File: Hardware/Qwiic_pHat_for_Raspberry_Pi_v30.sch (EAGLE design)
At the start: 26 parts, among them J1 Qwiic Right Angle, J10 RASPBERRYPI-40-PIN-GPIO_PTH_N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, J8 Qwiic Right Angle

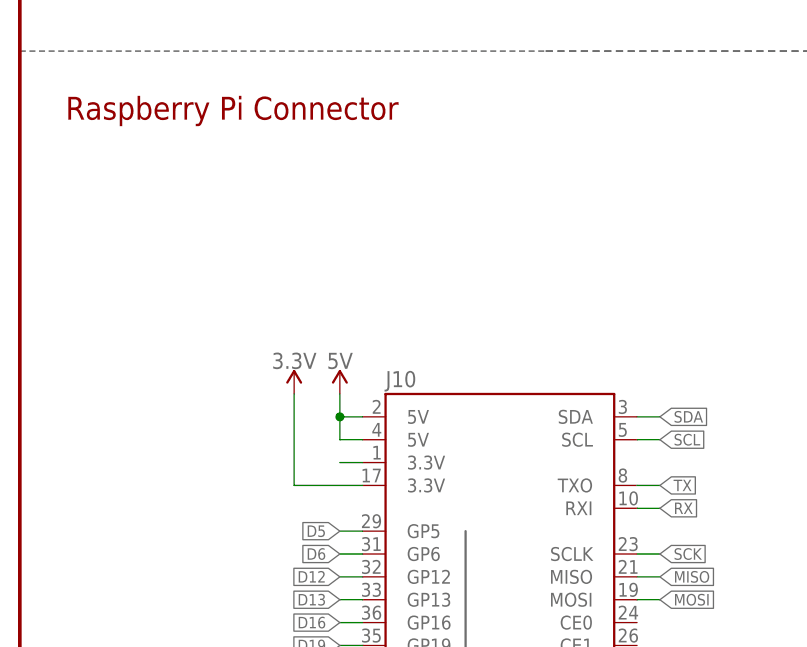
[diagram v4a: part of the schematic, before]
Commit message: Adds resettable 750mA fuse to 5V power line
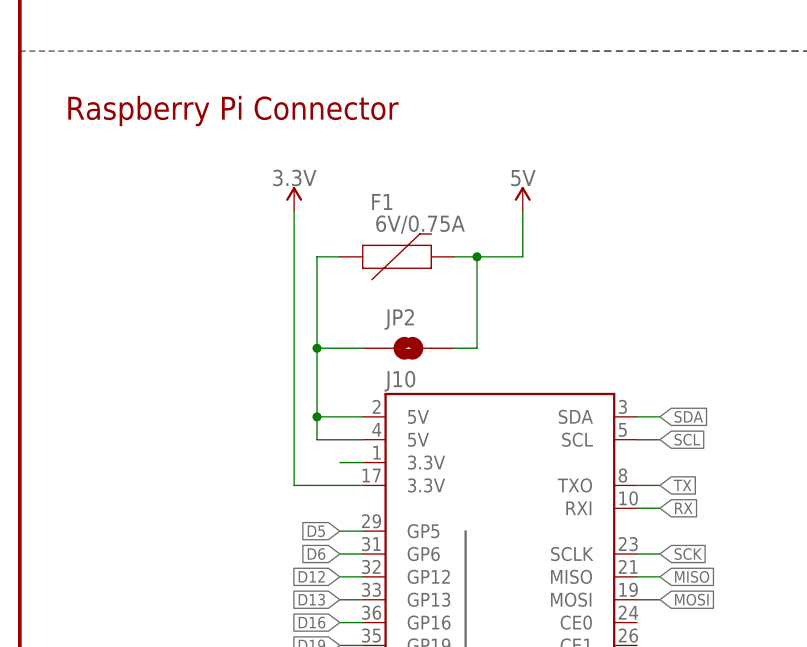
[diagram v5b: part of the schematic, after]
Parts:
- added F1: 6V/0.75A, SparkFun-Fuses:PPTC_0.75A
- added JP2: JUMPER-SMT_2_NO_NO-SILK, SparkFun-Jumpers:JUMPER-SMT_2_NO_NO-SILK
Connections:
- new net N$2: F1.1, J10.5V@2, J10.5V@4, JP2.1
- net 5V: now also F1.2, JP2.2; no longer J10.5V@2, J10.5V@4
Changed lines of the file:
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@@
 <?xml version="1.0" encoding="utf-8"?>
 <!DOCTYPE eagle SYSTEM "eagle.dtd">
-<eagle version="9.4.0">
+<eagle version="9.4.2">
 <drawing>
 <settings>
@@
 <part name="SUPPLY6" library="SparkFun-PowerSymbols" deviceset="3.3V" device=""/>
 <part name="J5" library="SparkFun-Connectors" deviceset="CONN_02" device="3.5MM-NO_SILK"/>
+<part name="F1" library="SparkFun-Fuses" deviceset="PPTC" device="_0.75A" value="6V/0.75A"/>
+<part name="JP2" library="SparkFun-Jumpers" deviceset="JUMPER-SMT_2_NO" device="_NO-SILK"/>
 </parts>
 <sheets>
@@
 <attribute name="VALUE" x="40.64" y="30.48" size="1.778" layer="96"/>
 </instance>
-<instance part="SUPPLY9" gate="G$1" x="35.56" y="93.98" smashed="yes">
-<attribute name="VALUE" x="35.56" y="96.774" size="1.778" layer="96" align="bottom-center"/>
+<instance part="SUPPLY9" gate="G$1" x="55.88" y="114.3" smashed="yes">
+<attribute name="VALUE" x="55.88" y="117.094" size="1.778" layer="96" align="bottom-center"/>
 </instance>
 <instance part="GND9" gate="1" x="35.56" y="25.4" smashed="yes">
@@
 <attribute name="VALUE" x="53.34" y="145.796" size="1.778" layer="96" font="vector" align="top-center"/>
 </instance>
-<instance part="SUPPLY2" gate="G$1" x="30.48" y="93.98" smashed="yes">
-<attribute name="VALUE" x="30.48" y="96.774" size="1.778" layer="96" align="bottom-center"/>
+<instance part="SUPPLY2" gate="G$1" x="30.48" y="114.3" smashed="yes">
+<attribute name="VALUE" x="30.48" y="117.094" size="1.778" layer="96" align="bottom-center"/>
 </instance>
 <instance part="J2" gate="G$1" x="160.02" y="157.48" smashed="yes" rot="R180">
@@
 <attribute name="VALUE" x="137.16" y="162.306" size="1.778" layer="96" font="vector" rot="MR180"/>
 <attribute name="NAME" x="137.16" y="151.892" size="1.778" layer="95" font="vector" rot="MR180"/>
+</instance>
+<instance part="F1" gate="F1" x="40.64" y="109.22" smashed="yes">
+<attribute name="NAME" x="40.259" y="116.205" size="1.778" layer="95" font="vector" rot="R180" align="bottom-center"/>
+<attribute name="VALUE" x="44.45" y="112.014" size="1.778" layer="96" font="vector" rot="R180" align="top-center"/>
+</instance>
+<instance part="JP2" gate="G$1" x="43.18" y="99.06" smashed="yes">
+<attribute name="NAME" x="40.64" y="101.6" size="1.778" layer="95" font="vector"/>
 </instance>
 </instances>
@@
 <segment>
 <pinref part="SUPPLY2" gate="G$1" pin="3.3V"/>
-<wire x1="30.48" y1="83.82" x2="30.48" y2="93.98" width="0.1524" layer="91"/>
+<wire x1="30.48" y1="83.82" x2="30.48" y2="114.3" width="0.1524" layer="91"/>
 <pinref part="J10" gate="G$1" pin="3.3V@17"/>
 <wire x1="38.1" y1="83.82" x2="30.48" y2="83.82" width="0.1524" layer="91"/>
@@
 <net name="5V" class="0">
 <segment>
-<pinref part="J10" gate="G$1" pin="5V@2"/>
-<wire x1="38.1" y1="91.44" x2="35.56" y2="91.44" width="0.1524" layer="91"/>
-<wire x1="35.56" y1="91.44" x2="35.56" y2="93.98" width="0.1524" layer="91"/>
-<pinref part="J10" gate="G$1" pin="5V@4"/>
-<wire x1="38.1" y1="88.9" x2="35.56" y2="88.9" width="0.1524" layer="91"/>
-<wire x1="35.56" y1="88.9" x2="35.56" y2="91.44" width="0.1524" layer="91"/>
-<junction x="35.56" y="91.44"/>
-<pinref part="SUPPLY9" gate="G$1" pin="5V"/>
-</segment>
-<segment>
 <pinref part="J2" gate="G$1" pin="1"/>
 <wire x1="152.4" y1="157.48" x2="149.86" y2="157.48" width="0.1524" layer="91"/>
@@
 <junction x="149.86" y="157.48"/>
 </segment>
+<segment>
+<pinref part="F1" gate="F1" pin="2"/>
+<pinref part="SUPPLY9" gate="G$1" pin="5V"/>
+<wire x1="48.26" y1="109.22" x2="50.8" y2="109.22" width="0.1524" layer="91"/>
+<pinref part="JP2" gate="G$1" pin="2"/>
+<wire x1="50.8" y1="109.22" x2="50.8" y2="99.06" width="0.1524" layer="91"/>
+<wire x1="50.8" y1="99.06" x2="48.26" y2="99.06" width="0.1524" layer="91"/>
+<junction x="50.8" y="109.22"/>
+<wire x1="50.8" y1="109.22" x2="55.88" y2="109.22" width="0.1524" layer="91"/>
+<wire x1="55.88" y1="109.22" x2="55.88" y2="114.3" width="0.1524" layer="91"/>
+</segment>
 </net>
 <net name="RX" class="0">
@@
 </segment>
 </net>
+<net name="N$2" class="0">
+<segment>
+<pinref part="J10" gate="G$1" pin="5V@2"/>
+<pinref part="J10" gate="G$1" pin="5V@4"/>
+<pinref part="F1" gate="F1" pin="1"/>
+<wire x1="35.56" y1="109.22" x2="33.02" y2="109.22" width="0.1524" layer="91"/>
+<wire x1="33.02" y1="109.22" x2="33.02" y2="99.06" width="0.1524" layer="91"/>
+<wire x1="33.02" y1="99.06" x2="33.02" y2="91.44" width="0.1524" layer="91"/>
+<wire x1="33.02" y1="91.44" x2="33.02" y2="88.9" width="0.1524" layer="91"/>
+<wire x1="33.02" y1="88.9" x2="38.1" y2="88.9" width="0.1524" layer="91"/>
+<wire x1="38.1" y1="91.44" x2="33.02" y2="91.44" width="0.1524" layer="91"/>
+<junction x="33.02" y="91.44"/>
+<pinref part="JP2" gate="G$1" pin="1"/>
+<wire x1="38.1" y1="99.06" x2="33.02" y2="99.06" width="0.1524" layer="91"/>
+<junction x="33.02" y="99.06"/>
+</segment>
+</net>

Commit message: Updates the silk
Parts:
- removed J10: RASPBERRYPI-40-PIN-GPIO_PTH_NO_SHROUD, SparkFun-Connectors:RASPBERRYPI-40-PIN-GPIO_PTH_NO_SHROUD
- added J6: (no value), SparkFun-Connectors:QWIIC_CONNECTOR
- J1: value Qwiic Right Angle -> RASPBERRYPI-40-PIN-GPIO_PTH_NO_SHROUD; device SparkFun-Connectors:I2C_STANDARDQWIIC -> SparkFun-Connectors:RASPBERRYPI-40-PIN-GPIO_PTH_NO_SHROUD
- J2: device SparkFun-Connectors:CONN_023.5MM -> SparkFun-Connectors:CONN_023.5MM-NO_SILK
- J3: device SparkFun-Connectors:QWIIC_CONNECTOR -> SparkFun-Connectors:CONN_023.5MM
- J4: value (none) -> Qwiic Right Angle; device SparkFun-Connectors:QWIIC_CONNECTOR -> SparkFun-Connectors:I2C_STANDARDQWIIC
- J5: device SparkFun-Connectors:CONN_023.5MM-NO_SILK -> SparkFun-Connectors:QWIIC_CONNECTOR
- JP1: value PULLUP -> JUMPER-SMT_2_NO_SILK; device SparkFun-Jumpers:JUMPER-SMT_3_2-NC_TRACE_NO-SILK -> SparkFun-Jumpers:JUMPER-SMT_2_NO_SILK
- JP2: value JUMPER-SMT_2_NO_NO-SILK -> PULLUP; device SparkFun-Jumpers:JUMPER-SMT_2_NO_NO-SILK -> SparkFun-Jumpers:JUMPER-SMT_3_2-NC_TRACE_NO-SILK
- LOGO1: value SFE_LOGO_NAME_FLAME.1_INCH -> REVISION; device SparkFun-Aesthetics:SFE_LOGO_NAME_FLAME.1_INCH -> SparkFun-Aesthetics:REVISION
- LOGO2: value REVISION -> OSHW-LOGOS; device SparkFun-Aesthetics:REVISION -> SparkFun-Aesthetics:OSHW-LOGOS
- LOGO3: value OSHW-LOGOS -> SFE_LOGO_NAME_FLAME.1_INCH; device SparkFun-Aesthetics:OSHW-LOGOS -> SparkFun-Aesthetics:SFE_LOGO_NAME_FLAME.1_INCH
- renumbered J8 to J7
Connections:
- net 3.3V: now also J1.3.3V@17, J5.2, J6.2, JP2.2; no longer J1.2, J10.3.3V@17, J3.2, JP1.2
- net 5V: now also J3.1, JP1.2; no longer J5.1, JP2.2
- net BUTTON/D17: now also J1.GP17; no longer J10.GP17
- net D12: now also J1.GP12; no longer J10.GP12
- net D13: now also J1.GP13; no longer J10.GP13
- net D16: now also J1.GP16; no longer J10.GP16
- net D18: now also J1.GP18#; no longer J10.GP18#
- net D19: now also J1.GP19; no longer J10.GP19
- net D20: now also J1.GP20; no longer J10.GP20
- net D21: now also J1.GP21; no longer J10.GP21
- net D22: now also J1.GP22; no longer J10.GP22
- net D23: now also J1.GP23; no longer J10.GP23
- net D24: now also J1.GP24; no longer J10.GP24
- net D25: now also J1.GP25; no longer J10.GP25
- net D26: now also J1.GP26; no longer J10.GP26
- net D27: now also J1.GP27; no longer J10.GP27
- net D4: now also J1.GP4; no longer J10.GP4
- net D5: now also J1.GP5; no longer J10.GP5
- net D6: now also J1.GP6; no longer J10.GP6
- net GND: now also J1.GND@14, J1.GND@20, J1.GND@25, J1.GND@30, J1.GND@34, J1.GND@39, J1.GND@6, J1.GND@9, J3.2, J5.1, J6.1; no longer J1.1, J10.GND@14, J10.GND@20, J10.GND@25, J10.GND@30, J10.GND@34, J10.GND@39, J10.GND@6, J10.GND@9, J3.1, J5.2
- net ID_SCL: now also J1.ID_SC; no longer J10.ID_SC
- net ID_SDA: now also J1.ID_SD; no longer J10.ID_SD
- net MISO: now also J1.MISO; no longer J10.MISO
- net MOSI: now also J1.MOSI; no longer J10.MOSI
- net N$1: now also J1.3.3V@1; no longer J10.3.3V@1
- net N$2: now also J1.5V@2, J1.5V@4, JP1.1; no longer J10.5V@2, J10.5V@4, JP2.1
- net N$3: now also JP2.3; no longer JP1.3
- net N$4: now also JP2.1; no longer JP1.1
- net RX: now also J1.RXI; no longer J10.RXI
- net SCK: now also J1.SCLK; no longer J10.SCLK
- net SCL: now also J1.SCL, J5.4, J6.4; no longer J1.4, J10.SCL, J3.4
- net SDA: now also J1.SDA, J5.3, J6.3; no longer J1.3, J10.SDA, J3.3
- net TX: now also J1.TXO; no longer J10.TXO
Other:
- note added: "Fuse Bypass"
- moved on the sheet: J2, J4
